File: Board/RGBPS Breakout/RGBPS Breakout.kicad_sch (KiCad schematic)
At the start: 11 parts, among them IC1 APDS-9999, J1 Conn_01x04_Pin, J2 Conn_01x01_Pin

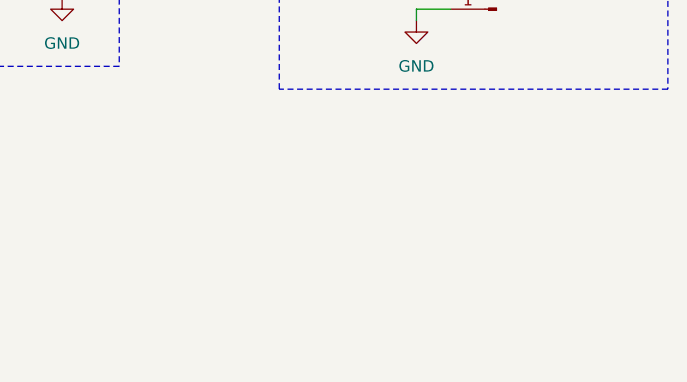
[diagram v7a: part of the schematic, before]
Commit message: start routing, add zone fill for ground
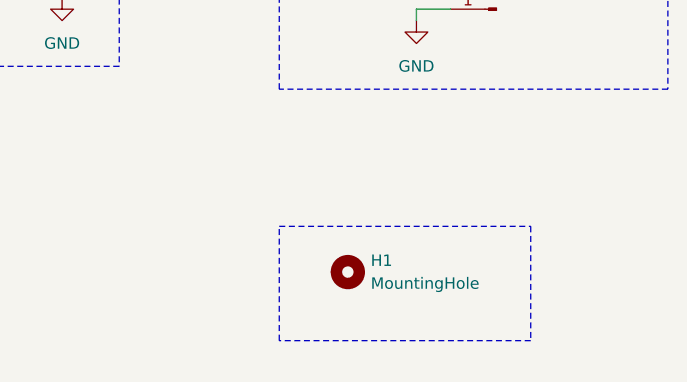
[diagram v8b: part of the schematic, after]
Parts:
- added H1: MountingHole, MountingHole:MountingHole_2.5mm, symbol Mechanical:MountingHole
- IC1: footprint SON65P200X200X75-6N-D -> (none)
- J2: footprint Connector_PinHeader_2.54mm:PinHeader_1x01_P2.54mm_Horizontal -> Connector_PinHeader_2.54mm:PinHeader_1x01_P2.54mm_Vertical
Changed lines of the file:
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@@
+	)
+	(rectangle
+		(start 218.44 127)
+		(end 246.38 139.7)
+		(stroke
+			(width 0)
+			(type dash)
+		)
+		(fill
+			(type none)
+		)
 	)
 	(rectangle
@@
 	)
 	(symbol
+		(lib_id "Mechanical:MountingHole")
+		(at 226.06 132.08 0)
+		(unit 1)
+		(exclude_from_sim yes)
+		(in_bom no)
+		(on_board yes)
+		(dnp no)
+		(fields_autoplaced yes)
+		(property "Reference" "H1"
+			(at 228.6 130.8099 0)
+			(effects
+				(font
+					(size 1.27 1.27)
+				)
+				(justify left)
+			)
+		)
+		(property "Value" "MountingHole"
+			(at 228.6 133.3499 0)
+			(effects
+				(font
+					(size 1.27 1.27)
+				)
+				(justify left)
+			)
+		)
+		(property "Footprint" "MountingHole:MountingHole_2.5mm"
+			(at 226.06 132.08 0)
+			(effects
+				(font
+					(size 1.27 1.27)
+				)
+				(hide yes)
+			)
+		)
+		(property "Datasheet" "~"
+			(at 226.06 132.08 0)
+			(effects
+				(font
+					(size 1.27 1.27)
+				)
+				(hide yes)
+			)
+		)
+		(property "Description" "Mounting Hole without connection"
+			(at 226.06 132.08 0)
+			(effects
+				(font
+					(size 1.27 1.27)
+				)
+				(hide yes)
+			)
+		)
+		(instances
+			(project "RGBPS Breakout"
+				(path "/ef8d1498-06d2-44f8-a4a9-e0c3d83a66fa"
+					(reference "H1")
+					(unit 1)
+				)
+			)
+		)
+	)
+	(symbol
 		(lib_id "Device:LED")
 		(at 175.26 100.33 0)
@@
 			)
 		)
-		(property "Footprint" "Connector_PinHeader_2.54mm:PinHeader_1x01_P2.54mm_Horizontal"
+		(property "Footprint" "Connector_PinHeader_2.54mm:PinHeader_1x01_P2.54mm_Vertical"
 			(at 242.57 90.17 0)
 			(effects
@@
 			)
 		)
-		(property "Footprint" "SON65P200X200X75-6N-D"
+		(property "Footprint" ""
 			(at 99.06 195.25 0)
 			(effects
